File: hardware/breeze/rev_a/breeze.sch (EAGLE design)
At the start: 7 parts, among them J1 SH_MALE_1X3/1MM-RA, J2 SH_MALE_1X3/1MM-TOP, J3 IMPULSE_GECKO_HEADER, Q1 NX3008PBK

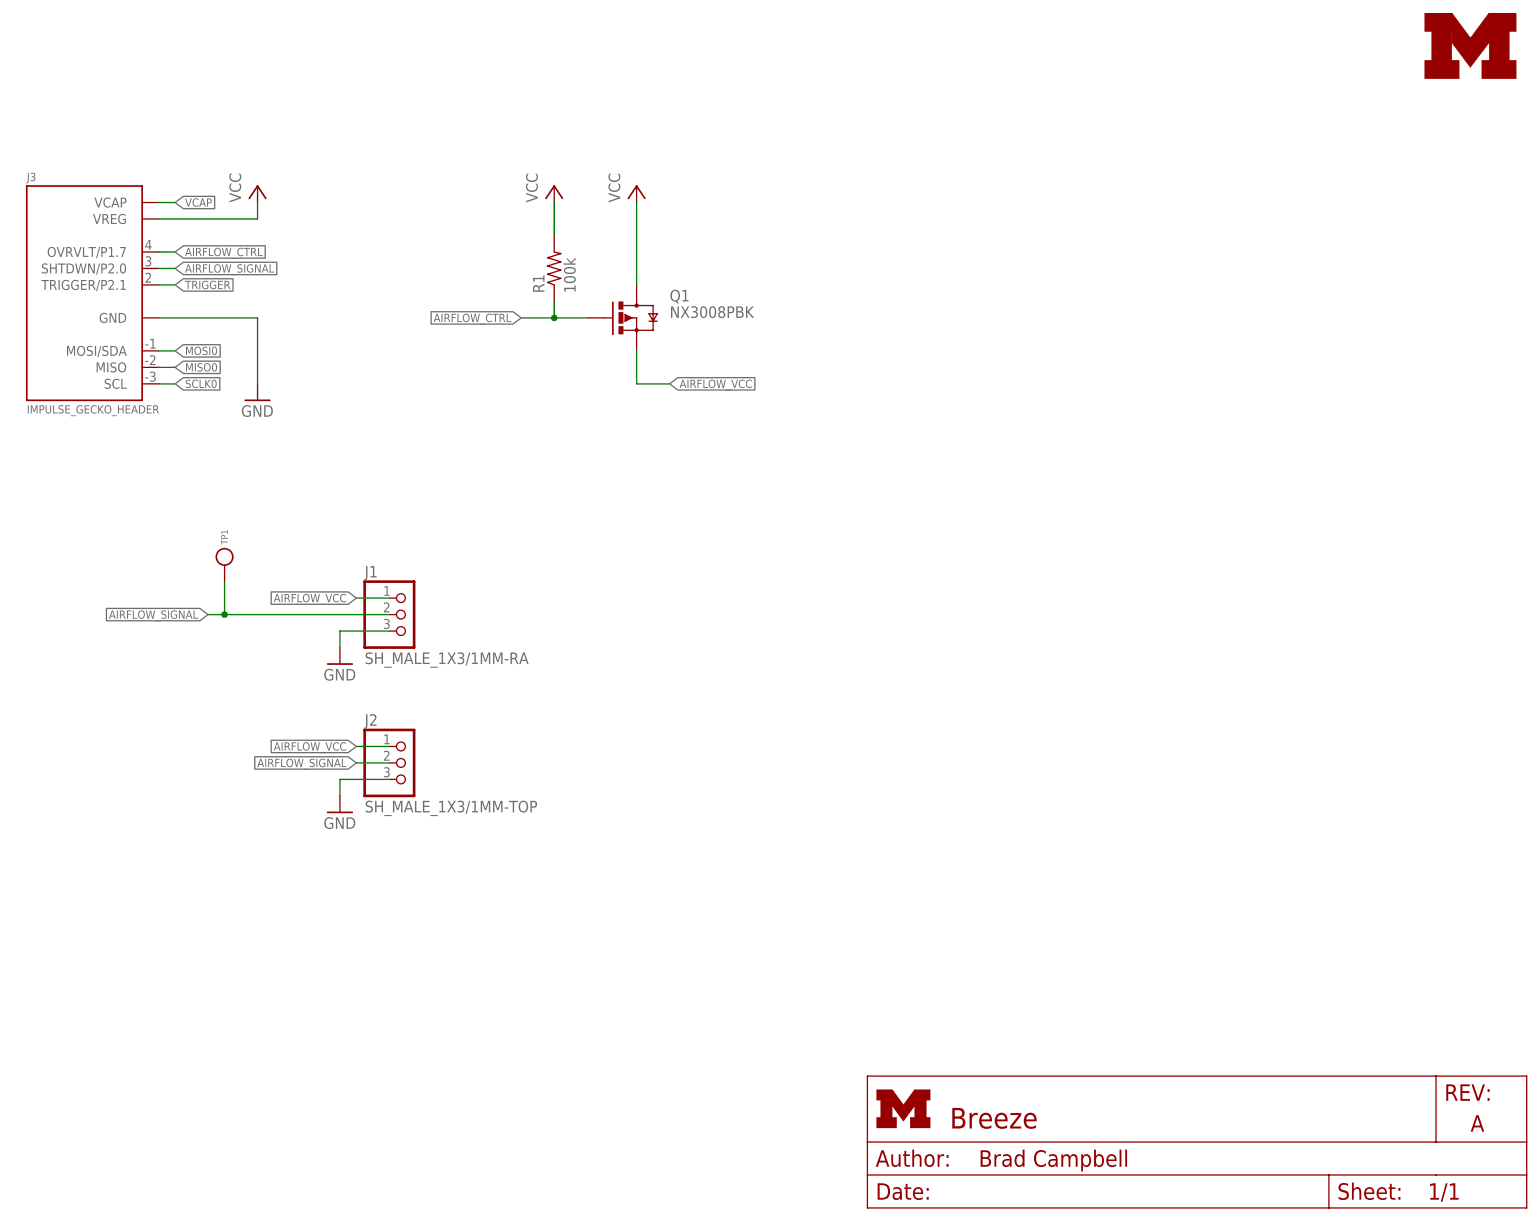
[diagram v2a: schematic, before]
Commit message: updated breeze with low pass filter
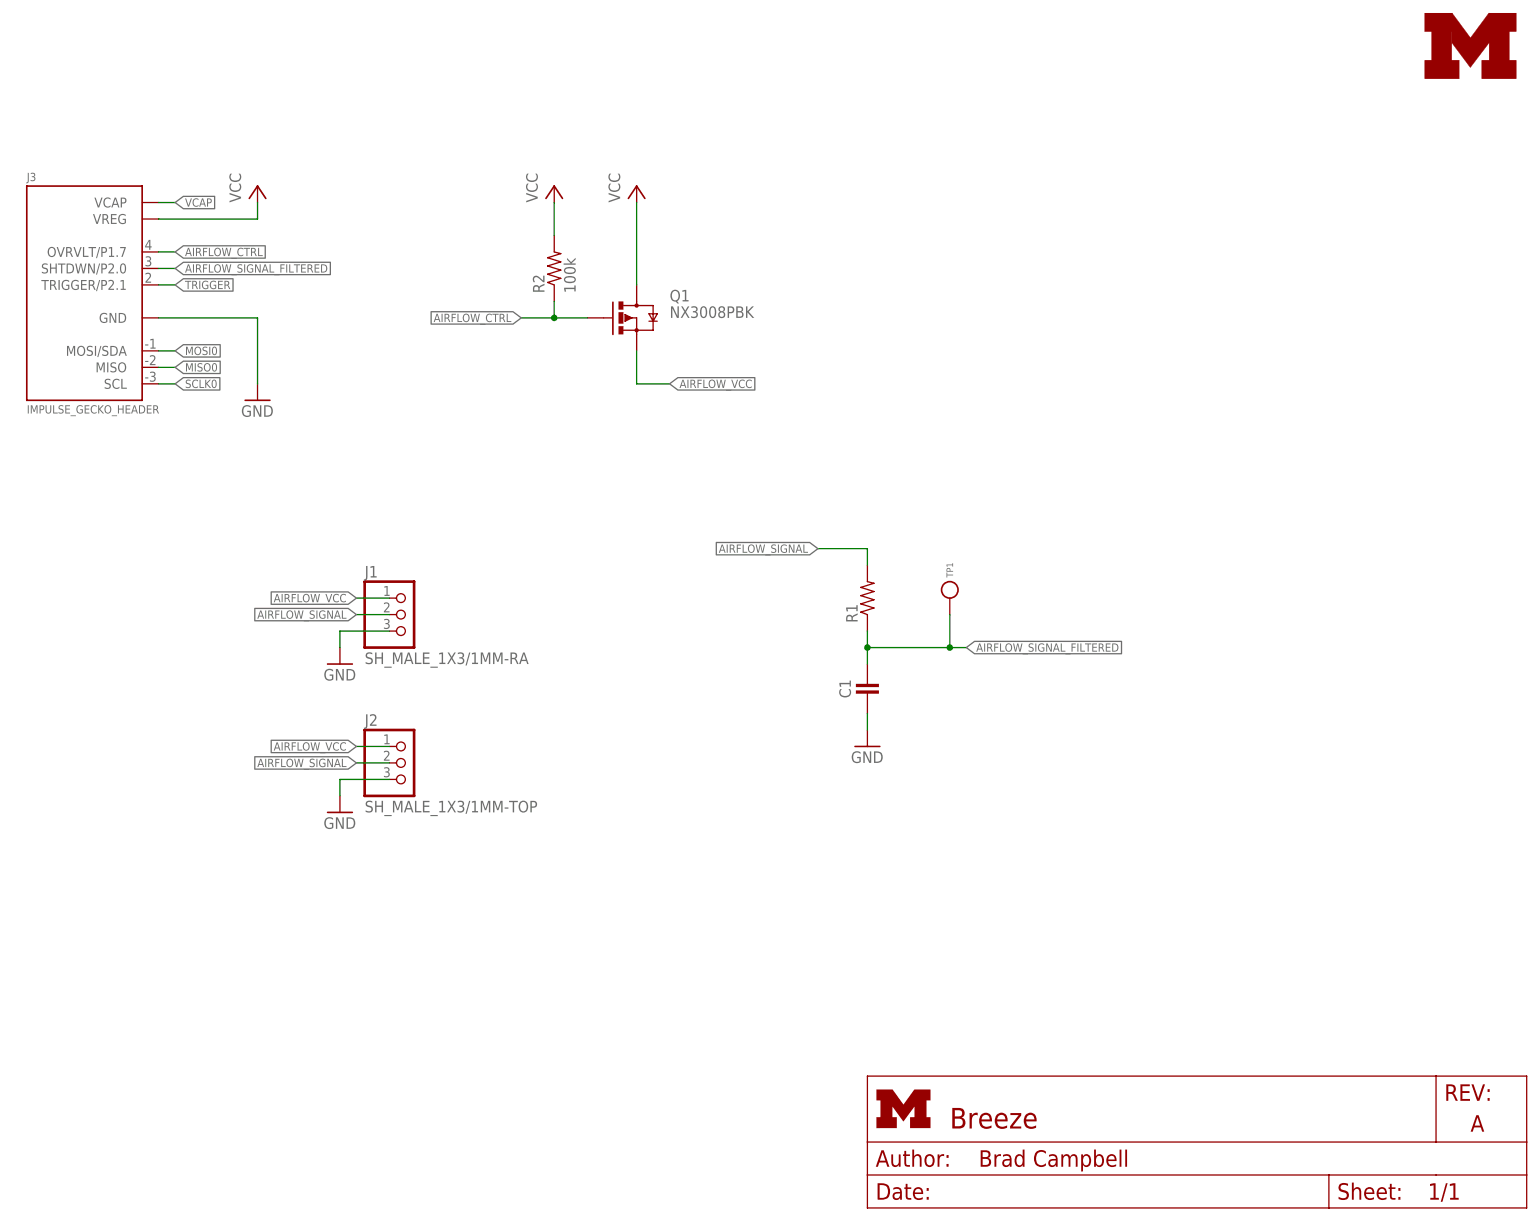
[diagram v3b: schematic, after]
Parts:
- added C1: (no value), passives:CAPACITOR
- added R2: 100k, passives:RESISTOR0402_RES
- R1: value 100k -> (none); device rcl:R-US_R0603 -> passives:RESISTOR0402_RES
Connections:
- new net AIRFLOW_SIGNAL_FILTERED: C1.1, J3.SHTDWN/P2.0, R1.1, TP1.TESTPOINT
- net AIRFLOW_CTRL: now also R2.1; no longer R1.1
- net AIRFLOW_SIGNAL: now also R1.2; no longer J3.SHTDWN/P2.0, TP1.TESTPOINT
- net GND: now also C1.2
- net VCC: now also R2.2; no longer R1.2
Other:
- moved on the sheet: R1, TP1
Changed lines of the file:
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@@
 <part name="LOGO1" library="logos" deviceset="UMICH_SOLID" device="_TINY"/>
 <part name="Q1" library="fets" deviceset="NX3008PBK" device=""/>
-<part name="R1" library="rcl" deviceset="R-US_" device="R0603" value="100k"/>
 <part name="P+3" library="supply1" deviceset="VCC" device=""/>
 <part name="P+4" library="supply1" deviceset="VCC" device=""/>
@@
 <part name="GND3" library="supply1" deviceset="GND" device=""/>
 <part name="TP1" library="headers" deviceset="TEST_POINT_0.040IN" device=""/>
+<part name="GND4" library="supply1" deviceset="GND" device=""/>
+<part name="C1" library="passives" deviceset="CAPACITOR" device=""/>
+<part name="R1" library="passives" deviceset="RESISTOR" device="0402_RES"/>
+<part name="R2" library="passives" deviceset="RESISTOR" device="0402_RES" value="100k"/>
 </parts>
 <sheets>
@@
 <instance part="LOGO1" gate="G$1" x="233.172" y="173.99"/>
 <instance part="Q1" gate="G$1" x="111.76" y="137.16"/>
-<instance part="R1" gate="G$1" x="99.06" y="144.78" rot="R90"/>
 <instance part="P+3" gate="VCC" x="99.06" y="157.48"/>
 <instance part="P+4" gate="VCC" x="111.76" y="157.48"/>
@@
 <instance part="GND2" gate="1" x="66.04" y="83.82"/>
 <instance part="GND3" gate="1" x="66.04" y="60.96"/>
-<instance part="TP1" gate="G$1" x="48.26" y="99.06" rot="R270"/>
+<instance part="TP1" gate="G$1" x="160.02" y="93.98" rot="R270"/>
+<instance part="GND4" gate="1" x="147.32" y="71.12"/>
+<instance part="C1" gate="G$1" x="147.32" y="81.28"/>
+<instance part="R1" gate="G$1" x="147.32" y="93.98" rot="R90"/>
+<instance part="R2" gate="G$1" x="99.06" y="144.78" rot="R90"/>
 </instances>
 <busses>
@@
 <pinref part="GND3" gate="1" pin="GND"/>
 </segment>
+<segment>
+<wire x1="147.32" y1="76.2" x2="147.32" y2="73.66" width="0.1524" layer="91"/>
+<pinref part="GND4" gate="1" pin="GND"/>
+<pinref part="C1" gate="G$1" pin="2"/>
+</segment>
 </net>
 <net name="VCC" class="0">
@@
 </segment>
 <segment>
-<pinref part="R1" gate="G$1" pin="2"/>
 <wire x1="99.06" y1="149.86" x2="99.06" y2="154.94" width="0.1524" layer="91"/>
 <pinref part="P+3" gate="VCC" pin="VCC"/>
+<pinref part="R2" gate="G$1" pin="2"/>
 </segment>
 <segment>
@@
 </segment>
 <segment>
-<pinref part="R1" gate="G$1" pin="1"/>
 <wire x1="99.06" y1="139.7" x2="99.06" y2="137.16" width="0.1524" layer="91"/>
 <pinref part="Q1" gate="G$1" pin="G"/>
@@
 <junction x="99.06" y="137.16"/>
 <label x="93.98" y="137.16" size="1.27" layer="95" rot="R180" xref="yes"/>
+<pinref part="R2" gate="G$1" pin="1"/>
 </segment>
 </net>
@@
 <segment>
 <pinref part="J1" gate="G$1" pin="2"/>
-<wire x1="73.66" y1="91.44" x2="48.26" y2="91.44" width="0.1524" layer="91"/>
-<label x="45.72" y="91.44" size="1.27" layer="95" rot="R180" xref="yes"/>
-<pinref part="TP1" gate="G$1" pin="TESTPOINT"/>
-<wire x1="48.26" y1="91.44" x2="45.72" y2="91.44" width="0.1524" layer="91"/>
-<wire x1="48.26" y1="96.52" x2="48.26" y2="91.44" width="0.1524" layer="91"/>
-<junction x="48.26" y="91.44"/>
+<wire x1="73.66" y1="91.44" x2="68.58" y2="91.44" width="0.1524" layer="91"/>
+<label x="68.58" y="91.44" size="1.27" layer="95" rot="R180" xref="yes"/>
 </segment>
 <segment>
@@
 </segment>
 <segment>
+<wire x1="147.32" y1="99.06" x2="147.32" y2="101.6" width="0.1524" layer="91"/>
+<wire x1="147.32" y1="101.6" x2="139.7" y2="101.6" width="0.1524" layer="91"/>
+<label x="139.7" y="101.6" size="1.27" layer="95" rot="R180" xref="yes"/>
+<pinref part="R1" gate="G$1" pin="2"/>
+</segment>
+</net>
+<net name="AIRFLOW_SIGNAL_FILTERED" class="0">
+<segment>
 <label x="40.64" y="144.78" size="1.27" layer="95" xref="yes"/>
 <pinref part="J3" gate="G$1" pin="SHTDWN/P2.0"/>
 <wire x1="40.64" y1="144.78" x2="38.1" y2="144.78" width="0.1524" layer="91"/>
 </segment>
+<segment>
+<wire x1="147.32" y1="88.9" x2="147.32" y2="86.36" width="0.1524" layer="91"/>
+<wire x1="147.32" y1="86.36" x2="147.32" y2="83.82" width="0.1524" layer="91"/>
+<wire x1="147.32" y1="86.36" x2="160.02" y2="86.36" width="0.1524" layer="91"/>
+<junction x="147.32" y="86.36"/>
+<pinref part="TP1" gate="G$1" pin="TESTPOINT"/>
+<wire x1="160.02" y1="86.36" x2="162.56" y2="86.36" width="0.1524" layer="91"/>
+<wire x1="160.02" y1="91.44" x2="160.02" y2="86.36" width="0.1524" layer="91"/>
+<junction x="160.02" y="86.36"/>
+<label x="162.56" y="86.36" size="1.27" layer="95" xref="yes"/>
+<pinref part="R1" gate="G$1" pin="1"/>
+<pinref part="C1" gate="G$1" pin="1"/>
+</segment>
 </net>
